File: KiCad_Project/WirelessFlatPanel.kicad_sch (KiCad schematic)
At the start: 18 parts, among them J1 JST-PH BAT Connector, J2 JST-XH LED Connector, J3 JST-XH Switch Connector, Q1 FQP30N06L, U1 TC1262-30, U2 U3V16F6, U3 LM3914N

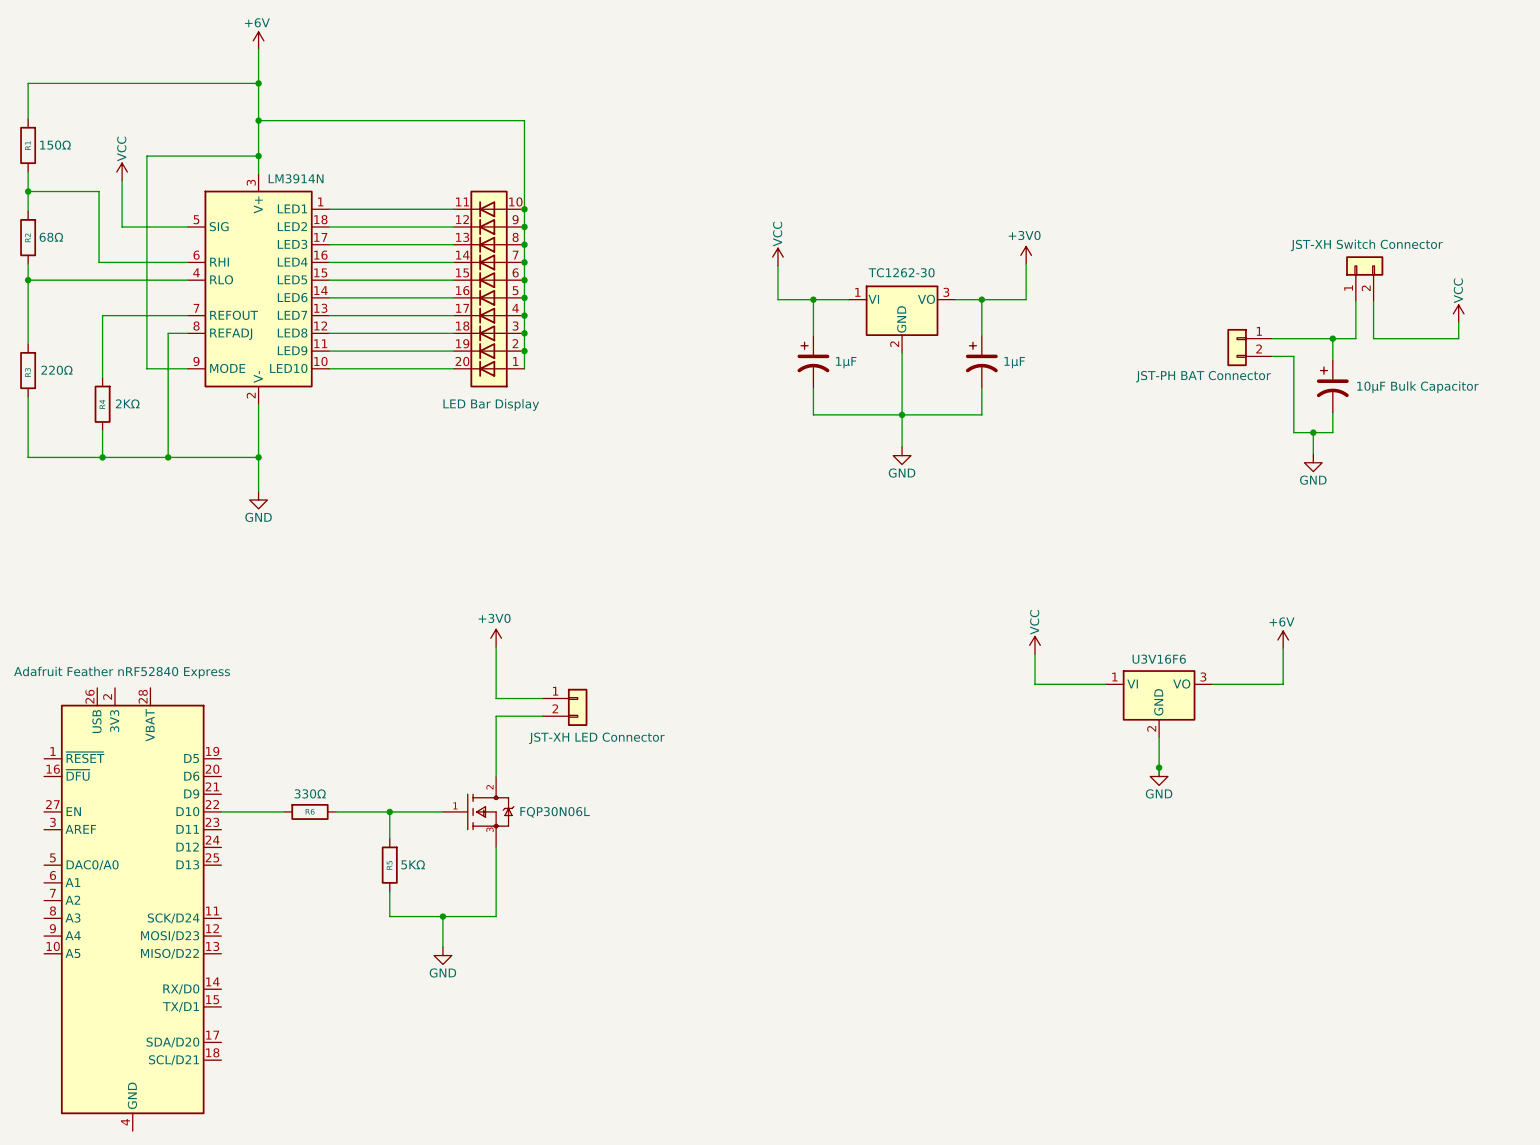
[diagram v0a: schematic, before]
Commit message: Updated KiCad project to greatly simplify wiring
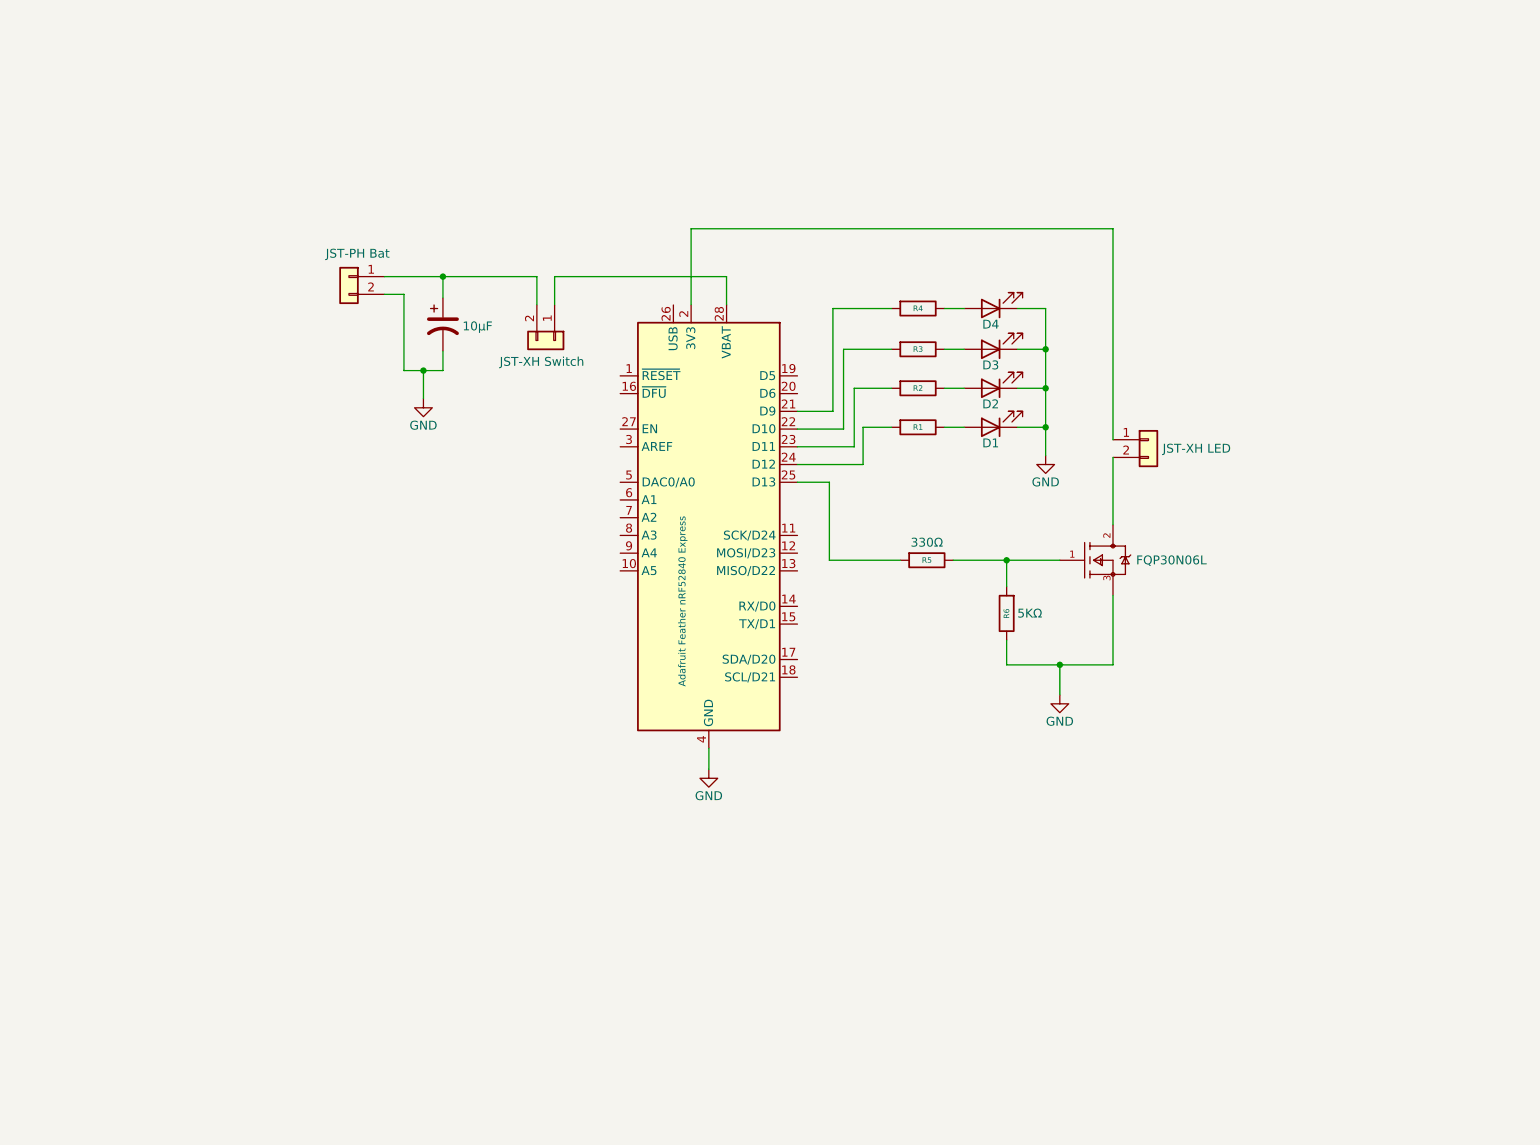
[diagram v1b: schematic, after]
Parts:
- removed BAR1: LED Bar Display, Display:HDSP-4830, symbol LED:HDSP-4830_2
- removed C1, C2: 1µF, Capacitor_THT:CP_Radial_D5.0mm_P2.50mm, symbol Device:C_Polarized_US
- removed J3: JST-XH Switch Connector, Connector_JST:JST_XH_B2B-XH-A_1x02_P2.50mm_Vertical, symbol Connector_Generic:Conn_01x02
- removed U1: TC1262-30, footprints:TC1262-3.0VAB, symbol Regulator_Linear:TC1262-30
- removed U2: U3V16F6, footprints:U3V16F6, symbol DarkSkyGeek_KiCad_Symbol_Library:U3V16F6
- removed U3: LM3914N, Package_DIP:DIP-18_W7.62mm, symbol Driver_LED:LM3914N
- added D1, D2, D3, D4: LED, LED_THT:LED_D5.0mm, symbol Device:LED
- added J2: JST-XH Switch, Connector_JST:JST_XH_B2B-XH-A_1x02_P2.50mm_Vertical, symbol Connector_Generic:Conn_01x02
- C1: renamed from C3; value 10µF Bulk Capacitor -> 10µF
- J1: value JST-PH BAT Connector -> JST-PH Bat
- J3: renamed from J2; value JST-XH LED Connector -> JST-XH LED
- R1: value 150Ω -> ?Ω
- R2: value 68Ω -> ?Ω
- R3: value 220Ω -> ?Ω
- R4: value 2KΩ -> ?Ω
- renumbered R6 to R5, R5 to R6
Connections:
- net +3V0 is gone; now on an unnamed net: J3.1 (Pin_1)
- net +6V is gone; now on an unnamed net: R1.2
- net GND: now also A1.4 (GND), D1.1 (K), D2.1 (K), D3.1 (K), D4.1 (K); no longer R3.1, R4.1
- net at R5.2: now also A1.25 (D13); no longer A1.22 (D10)
- net at R1.1: now also D1.2 (A); no longer R2.2
- net at A1.21 (D9): now also R4.2
- net at A1.23 (D11): now also R2.2
- net at A1.28 (VBAT): now also J2.1 (Pin_1)
- net at R2.1: now also D2.2 (A); no longer R3.2
- net at C1.1, J1.1 (Pin_1): now also J2.2 (Pin_2)
- new net: D3.2 (A), R3.1
- new net: A1.22 (D10), R3.2
- new net: D4.2 (A), R4.1
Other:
- moved on the sheet: R5, R6
